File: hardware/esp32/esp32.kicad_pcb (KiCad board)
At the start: 2 copper layers, 22 x 34.2 mm, 15 parts, among them J1 Conn_01x02, J2 Conn_01x02, J3 Conn_01x02, J4 Conn_01x02, J5 Conn_01x02, SW1 RESET, SW2 BOOT, U2 ESP32-S3-MINI-1-N8

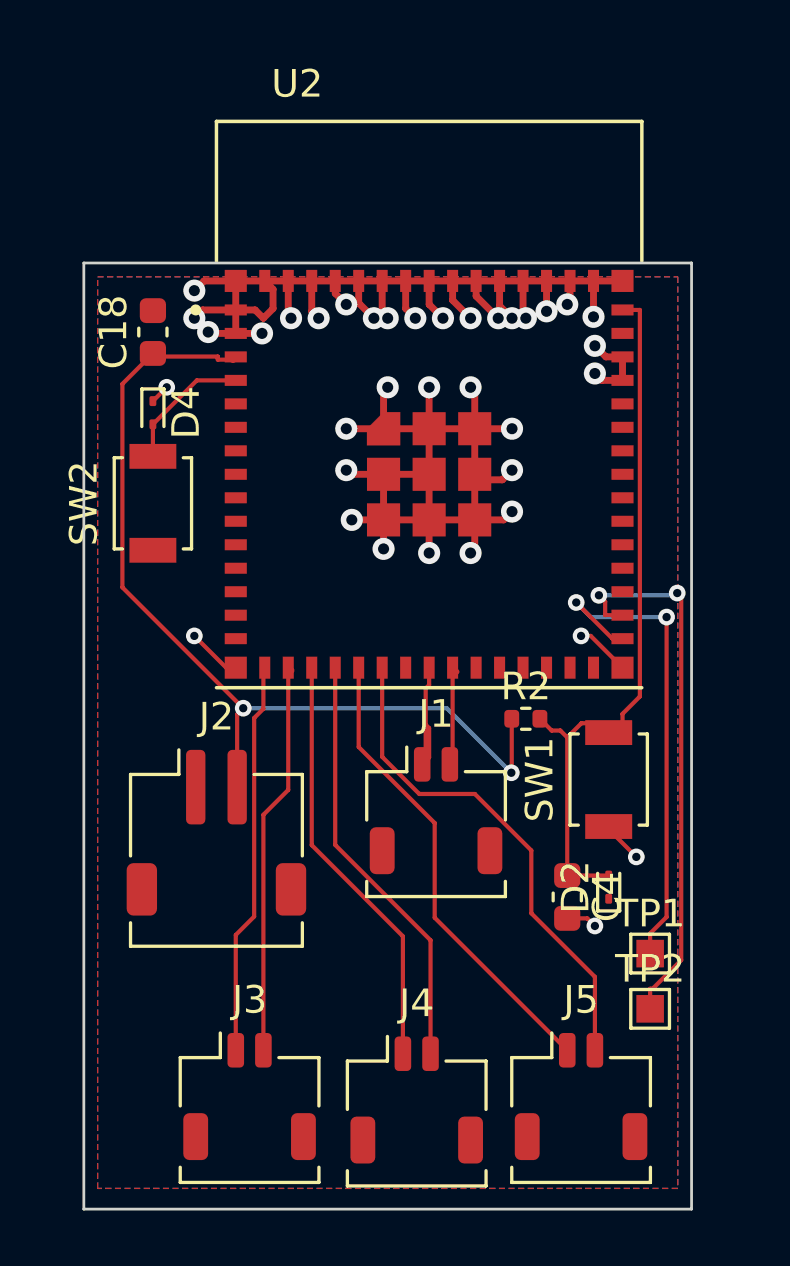
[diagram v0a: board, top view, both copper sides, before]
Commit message: simplify pins and buttons
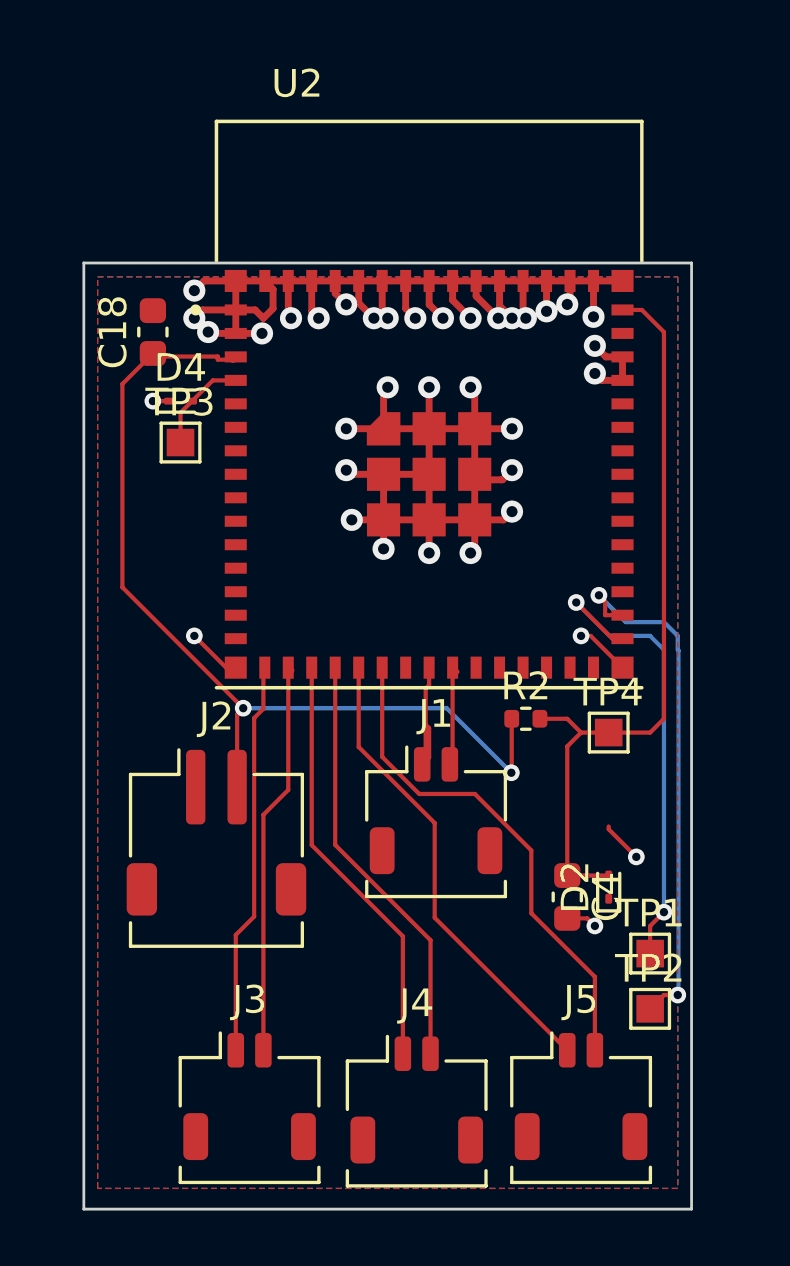
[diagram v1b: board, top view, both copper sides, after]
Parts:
- removed SW1: RESET, Button_Switch_SMD:SW_SPST_B3U-1000P
- removed SW2: BOOT, Button_Switch_SMD:SW_SPST_B3U-1000P
- added TP3: TestPoint, TestPoint:TestPoint_Pad_1.0x1.0mm, F.Cu at (104.0, 39.0)
- added TP4: TestPoint, TestPoint:TestPoint_Pad_1.0x1.0mm, F.Cu at (119.5, 49.5)
- moved D4 1.08 mm to (104.0, 37.5), turned to 0 degrees
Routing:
- net /GPIO0: track 4.82 -> 3.56 mm
- net /ESP32_EN: track 26.6 -> 27.6 mm
- net Net-(U2-IO35): track 18.1 -> 17.3 mm
- net Net-(U2-IO36): track 19.9 -> 19.1 mm

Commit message: esp32 routing
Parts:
- removed J3, J4, J5: Conn_01x02, Connector_JST:JST_SHL_SM02B-SHLS-TF_1x02-1MP_P1.00mm_Horizontal
- removed TP1, TP2: TestPoint, TestPoint:TestPoint_Pad_1.0x1.0mm
- added J6: Conn_01x08, Connector_JST:JST_SHL_SM08B-SHLS-TF_1x08-1MP_P1.00mm_Horizontal, F.Cu at (114.0, 62.7)
- moved C4 2.64 mm to (119.5, 53.3)
- moved D2 2.64 mm to (121.0, 52.9)
- moved R2 2.51 mm to (118.0, 51.0)
- moved TP4 1.58 mm to (121.0, 50.0)
- moved TP3 1.50 mm to (104.0, 40.5)
- moved J1 0.70 mm to (113.5, 51.7)
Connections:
- U2 pad 15: unconnected-(U2-IO11-Pad15) -> Net-(J6-Pin_1)
- U2 pad 22: unconnected-(U2-IO18-Pad22) -> Net-(J6-Pin_8)
- U2 pad 31: Net-(U2-IO35) -> unconnected-(U2-IO35-Pad31)
- U2 pad 32: Net-(U2-IO36) -> unconnected-(U2-IO36-Pad32)
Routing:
- net Net-(J6-Pin_1): track 0.00 -> 28.0 mm, vias 0 -> 2
- net Net-(U2-IO36): track 19.1 -> 0.00 mm, vias 2 -> 0
- net Net-(J6-Pin_8): track 0.00 -> 18.2 mm
- net Net-(U2-IO35): track 17.3 -> 0.00 mm, vias 2 -> 0
- net Net-(J6-Pin_3): track 14.4 -> 18.9 mm, vias 0 -> 2
- net GND: track 86.6 -> 89.7 mm
- net /USB_D-: track 5.02 -> 2.85 mm
- net Net-(J6-Pin_2): track 14.3 -> 16.4 mm
- net Net-(J6-Pin_7): track 18.2 -> 16.4 mm, vias 0 -> 2
- net /ESP32_EN: track 27.6 -> 25.8 mm
- net /GPIO0: track 3.56 -> 5.13 mm
- net Net-(J6-Pin_6): track 17.0 -> 16.0 mm, vias 0 -> 2
- net /USB_D+: track 3.75 -> 3.02 mm
- net +3V3: track 34.1 -> 34.6 mm
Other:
- board size 22 x 34.2 mm -> 21.5 x 34.2 mm

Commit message: esp32
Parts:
- added TP1: TestPoint, MountingHole:MountingHole_2.1mm, F.Cu at (104.5, 62.5)
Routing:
- net Net-(J6-Pin_1): track 28.0 -> 19.3 mm
- net Net-(J6-Pin_3): track 18.9 -> 15.8 mm
- net Net-(J6-Pin_2): track 16.4 -> 15.8 mm
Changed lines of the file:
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@@
 		)
+	)
+	(footprint "MountingHole:MountingHole_2.1mm"
+		(layer "F.Cu")
+		(at 104.5 62.5)
+		(descr "Mounting Hole 2.1mm, no annular, generated by kicad-footprint-generator mountinghole.py")
+		(tags "mountinghole")
+		(property "Reference" "TP1"
+			(at 0 -3.05 0)
+			(layer "F.SilkS")
+			(effects
+				(font
+					(size 1 1)
+					(thickness 0.15)
+				)
+			)
+		)
+		(property "Value" "TestPoint"
+			(at 0 3.05 0)
+			(layer "F.Fab")
+			(effects
+				(font
+					(size 1 1)
+					(thickness 0.15)
+				)
+			)
+		)
+		(property "Datasheet" "~"
+			(at 0 0 0)
+			(layer "F.Fab")
+			(hide yes)
+			(effects
+				(font
+					(size 1.27 1.27)
+					(thickness 0.15)
+				)
+			)
+		)
+		(property "Description" "test point"
+			(at 0 0 0)
+			(layer "F.Fab")
+			(hide yes)
+			(effects
+				(font
+					(size 1.27 1.27)
+					(thickness 0.15)
+				)
+			)
+		)
+		(property ki_fp_filters "Pin* Test*")
+		(sheetname "/")
+		(sheetfile "esp32.kicad_sch")
+		(attr exclude_from_pos_files)
+		(fp_circle
+			(center 0 0)
+			(end 2.1 0)
+			(stroke
+				(width 0.15)
+				(type solid)
+			)
+			(fill no)
+			(layer "Cmts.User")
+		)
+		(fp_circle
+			(center 0 0)
+			(end 2.35 0)
+			(stroke
+				(width 0.05)
+				(type solid)
+			)
+			(fill no)
+			(layer "F.CrtYd")
+		)
+		(fp_text user "${REFERENCE}"
+			(at 0 0 0)
+			(layer "F.Fab")
+			(effects
+				(font
+					(size 1 1)
+					(thickness 0.15)
+				)
+			)
+		)
+		(pad "" np_thru_hole circle
+			(at 0 0)
+			(size 2.1 2.1)
+			(drill 2.1)
+			(layers "*.Cu" "*.Mask")
+		)
+		(embedded_fonts no)
 	)
 	(footprint "Capacitor_SMD:C_0603_1608Metric"
@@
 	)
 	(segment
-		(start 109.4586 65.2609)
-		(end 108.6816 65.2609)
-		(width 0.1524)
-		(layer "F.Cu")
-		(net 33)
-	)
-	(segment
-		(start 110.5 64.2195)
-		(end 109.4586 65.2609)
-		(width 0.1524)
-		(layer "F.Cu")
-		(net 33)
-	)
-	(segment
 		(start 105.1348 45.5244)
 		(end 105.3721 45.7617)
@@
 	)
 	(segment
-		(start 108.6816 65.2609)
-		(end 105.3304 61.9097)
-		(width 0.1524)
-		(layer "F.Cu")
-		(net 33)
-	)
-	(segment
 		(start 105.3721 45.7617)
 		(end 105.3721 46.1)
@@
 	)
 	(segment
-		(start 110.5 61)
-		(end 110.5 64.2195)
+		(start 109.5 60)
+		(end 110.5 61)
 		(width 0.1524)
 		(layer "F.Cu")
@@
 	)
 	(segment
-		(start 105.3304 61.9097)
-		(end 105.3304 49.1591)
+		(start 109 60)
+		(end 109.5 60)
 		(width 0.1524)
 		(layer "F.Cu")
@@
 	)
 	(via
-		(at 105.3304 49.1591)
-		(size 0.6048)
+		(at 109 60)
+		(size 0.604799)
 		(drill 0.299999)
 		(layers "F.Cu" "B.Cu")
@@
 	)
 	(segment
-		(start 105.1348 48.9635)
-		(end 105.1348 45.5244)
+		(start 105.1348 45.5244)
+		(end 105.1348 56.1348)
 		(width 0.1524)
 		(layer "B.Cu")
@@
 	)
 	(segment
-		(start 105.3304 49.1591)
-		(end 105.1348 48.9635)
+		(start 105.1348 56.1348)
+		(end 107 58)
 		(width 0.1524)
 		(layer "B.Cu")
@@
 	)
 	(segment
-		(start 110.9374 59.3774)
-		(end 111.5 59.3774)
+		(start 107 58)
+		(end 109 60)
+		(width 0.1524)
+		(layer "B.Cu")
+		(net 33)
+	)
+	(segment
+		(start 107.05 55.9304)
+		(end 111.5 60.3804)
 		(width 0.1524)
 		(layer "F.Cu")
@@
 	)
 	(segment
-		(start 111.5 59.3774)
+		(start 111.5 60.3804)
 		(end 111.5 61)
-		(width 0.1524)
-		(layer "F.Cu")
-		(net 34)
-	)
-	(segment
-		(start 110.56 59)
-		(end 110.9374 59.3774)
-		(width 0.1524)
-		(layer "F.Cu")
-		(net 34)
-	)
-	(segment
-		(start 107.05 55.9304)
-		(end 110.12 59)
 		(width 0.1524)
 		(layer "F.Cu")
@@
 	)
 	(segment
-		(start 110.12 59)
-		(end 110.56 59)
-		(width 0.1524)
-		(layer "F.Cu")
-		(net 34)
-	)
-	(segment
 		(start 108 50.3314)
 		(end 108 47.25)
@@
 	)
 	(segment
-		(start 108 53.3759)
-		(end 108 53.294)
-		(width 0.1524)
-		(layer "F.Cu")
-		(net 35)
-	)
-	(segment
 		(start 112.5 59.2816)
 		(end 112.5 61)
@@
 	)
 	(segment
-		(start 108 53.2913)
-		(end 108 53.2068)
-		(width 0.1524)
-		(layer "F.Cu")
-		(net 35)
-	)
-	(segment
-		(start 108 53.2068)
-		(end 108 50.3314)
-		(width 0.1524)
-		(layer "F.Cu")
-		(net 35)
-	)
-	(segment
 		(start 107.9 50.4314)
 		(end 107.9 51.06)
 		(width 0.1524)
 		(layer "F.Cu")
-		(net 35)
-	)
-	(segment
-		(start 108 53.294)
-		(end 108 53.2913)
-		(width 0.1524)
-		(layer "F.Cu")

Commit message: esp32 rebuild connectors
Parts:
- removed J1: Conn_01x02, Connector_JST:JST_SHL_SM02B-SHLS-TF_1x02-1MP_P1.00mm_Horizontal
- removed J6: Conn_01x08, Connector_JST:JST_SHL_SM08B-SHLS-TF_1x08-1MP_P1.00mm_Horizontal
- removed TP1: TestPoint, MountingHole:MountingHole_2.1mm
- added J3: Conn_01x10, Connector_JST:JST_SHL_SM10B-SHLS-TF_1x10-1MP_P1.00mm_Horizontal, F.Cu at (115.5, 57.5)
- moved J2 3.37 mm to (104.8, 56.5)
- moved C4 3.04 mm to (119.0, 50.3)
- moved D2 0.92 mm to (120.9, 52.0), turned to 0 degrees
- moved R2 0.51 mm to (117.5, 51.0), turned to 90 degrees
- moved TP4 0.50 mm to (121.0, 50.5)
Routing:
- net /USB_D+: track 3.02 -> 11.4 mm
- net /USB_D-: track 2.85 -> 11.1 mm
- net Net-(J3-Pin_8): track 18.2 -> 11.1 mm
- net +3V3: track 34.6 -> 40.5 mm
- net Net-(J3-Pin_7): track 16.4 -> 11.0 mm, vias 2 -> 0
- net Net-(J3-Pin_1): track 19.3 -> 14.2 mm, vias 2 -> 0
- net Net-(J3-Pin_6): track 16.0 -> 10.9 mm, vias 2 -> 0
- net Net-(J3-Pin_2): track 15.8 -> 10.7 mm
- net Net-(J3-Pin_4): track 15.8 -> 10.8 mm
- net Net-(J3-Pin_5): track 15.9 -> 10.9 mm
- net Net-(J3-Pin_3): track 15.8 -> 10.9 mm, vias 2 -> 0
- net /ESP32_EN: track 25.8 -> 23.8 mm
- net GND: track 89.7 -> 91.3 mm
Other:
- board size 21.5 x 34.2 mm -> 22.5 x 29.8 mm

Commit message: some fixes
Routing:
- net GND: track 91.3 -> 93.1 mm
- net +3V3: track 40.5 -> 41.4 mm
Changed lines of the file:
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@@
 		(start 120.5 53)
 		(end 121 53.5)
-		(width 0.1524)
+		(width 0.3)
 		(layer "F.Cu")
 		(net 1)
@@
 		(start 119.95 52)
 		(end 119 51.05)
-		(width 0.1524)
+		(width 0.3)
 		(layer "F.Cu")
 		(net 1)
@@
 	)
 	(segment
+		(start 103.775 34.225)
+		(end 104.5 33.5)
+		(width 0.1524)
+		(layer "F.Cu")
+		(net 1)
+	)
+	(segment
 		(start 104.8 34.2)
 		(end 104.5 34.5)
@@
 	)
 	(segment
+		(start 103 34.225)
+		(end 103.775 34.225)
+		(width 0.1524)
+		(layer "F.Cu")
+		(net 1)
+	)
+	(segment
 		(start 118.1 33.15)
 		(end 118.95 33.15)
@@
 		(start 120.5 52)
 		(end 119.95 52)
-		(width 0.1524)
+		(width 0.3)
 		(layer "F.Cu")
 		(net 1)
@@
 		(start 102.5 53.3)
 		(end 102.5 52.5)
-		(width 0.1524)
+		(width 0.5)
 		(layer "F.Cu")
 		(net 1)
@@
 		(start 120.5 52)
 		(end 120.5 53)
-		(width 0.1524)
+		(width 0.3)
 		(layer "F.Cu")
 		(net 1)
@@
 		(start 104 54.8)
 		(end 102.5 53.3)
-		(width 0.1524)
+		(width 0.5)
 		(layer "F.Cu")
 		(net 1)
@@
 	)
 	(segment
-		(start 105.2129 52.9724)
+		(start 102 50)
+		(end 104.9724 52.9724)
+		(width 0.4)
+		(layer "F.Cu")
+		(net 32)
+	)
+	(segment
+		(start 105.5 54.8)
 		(end 105.5 53.2595)
-		(width 0.1524)
-		(layer "F.Cu")
-		(net 32)
-	)
-	(segment
-		(start 105.95 35.95)
-		(end 106 35.9)
-		(width 0.25)
-		(layer "F.Cu")
-		(net 32)
-	)
-	(segment
-		(start 103.275 35.95)
-		(end 103.225 36)
-		(width 0.1524)
-		(layer "F.Cu")
-		(net 32)
-	)
-	(segment
-		(start 105.5 53.2595)
-		(end 105.5 53.5257)
-		(width 0.1524)
-		(layer "F.Cu")
-		(net 32)
-	)
-	(segment
-		(start 103.225 36)
-		(end 103.112 35.8877)
-		(width 0.1524)
-		(layer "F.Cu")
-		(net 32)
-	)
-	(segment
-		(start 103.112 35.8875)
-		(end 103 35.775)
-		(width 0.1524)
-		(layer "F.Cu")
-		(net 32)
-	)
-	(segment
-		(start 117.5 51.6667)
-		(end 119.223 53.3897)
-		(width 0.1524)
-		(layer "F.Cu")
-		(net 32)
-	)
-	(segment
-		(start 105.5 53.5257)
-		(end 105.5 54.8)
-		(width 0.1524)
-		(layer "F.Cu")
-		(net 32)
-	)
-	(segment
-		(start 103.112 35.8877)
-		(end 103.112 35.8875)
-		(width 0.1524)
+		(width 0.5)
+		(layer "F.Cu")
+		(net 32)
+	)
+	(segment
+		(start 106 35.9)
+		(end 103.125 35.9)
+		(width 0.4)
+		(layer "F.Cu")
+		(net 32)
+	)
+	(segment
+		(start 102 36.775)
+		(end 102 50)
+		(width 0.4)
 		(layer "F.Cu")
 		(net 32)
@@
 	(segment
 		(start 103 35.775)
-		(end 103 35.7755)
-		(width 0.1524)
-		(layer "F.Cu")
-		(net 32)
-	)
-	(segment
-		(start 103 50.7595)
-		(end 103 35.7755)
-		(width 0.1524)
-		(layer "F.Cu")
-		(net 32)
-	)
-	(segment
-		(start 105.2129 52.9724)
-		(end 103 50.7595)
-		(width 0.1524)
-		(layer "F.Cu")
-		(net 32)
-	)
-	(segment
-		(start 105.9 36)
-		(end 105.95 35.95)
-		(width 0.25)
+		(end 102 36.775)
+		(width 0.4)
+		(layer "F.Cu")
+		(net 32)
+	)
+	(segment
+		(start 117.5191 51.52)
+		(end 119.3888 53.3897)
+		(width 0.4)
+		(layer "F.Cu")
+		(net 32)
+	)
+	(segment
+		(start 117.5 51.52)
+		(end 117.5191 51.52)
+		(width 0.1524)
 		(layer "F.Cu")
 		(net 32)
@@
 	)
 	(segment
-		(start 103 35.7755)
-		(end 103.112 35.8877)
-		(width 0.1524)
+		(start 104.9724 52.9724)
+		(end 105.2129 52.9724)
+		(width 0.4)
+		(layer "F.Cu")
+		(net 32)
+	)
+	(segment
+		(start 103.125 35.9)
+		(end 103 35.775)
+		(width 0.4)
+		(layer "F.Cu")
+		(net 32)
+	)
+	(segment
+		(start 105.5 53.2595)
+		(end 105.2129 52.9724)
+		(width 0.5)
 		(layer "F.Cu")
 		(net 32)
@@
 		(start 119.223 53.3897)
 		(end 119.3888 53.3897)
-		(width 0.1524)
-		(layer "F.Cu")
-		(net 32)
-	)
-	(segment
-		(start 105.95 35.95)
-		(end 103.275 35.95)
 		(width 0.1524)
 		(layer "F.Cu")
@@
 	)
 	(segment
-		(start 105.6302 53.3897)
-		(end 105.2129 52.9724)
-		(width 0.1524)
+		(start 105.2129 52.9724)
+		(end 118.9715 52.9724)
+		(width 0.4)
 		(layer "B.Cu")
 		(net 32)
 	)
 	(segment
-		(start 119.3888 53.3897)
-		(end 105.6302 53.3897)
-		(width 0.1524)
+		(start 118.9715 52.9724)
+		(end 119.3888 53.3897)
+		(width 0.4)
 		(layer "B.Cu")
 		(net 32)

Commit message: wip
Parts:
- removed TP3, TP4: TestPoint, TestPoint:TestPoint_Pad_1.0x1.0mm
- added J1: Conn_01x01, Connector_PinHeader_1.00mm:PinHeader_1x01_P1.00mm_Vertical, F.Cu at (121.0, 50.5)
- added J6: Conn_01x01, Connector_PinHeader_1.00mm:PinHeader_1x01_P1.00mm_Vertical, F.Cu at (103.5, 40.5)
- D2, D4: footprint Diode_SMD:D_SOD-923 -> Package_TO_SOT_SMD:SOT-723
- moved D2 1.65 mm to (121.4, 53.6), turned to -90 degrees
- moved D4 0.50 mm to (103.5, 37.5), turned to 90 degrees
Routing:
- net GND: track 93.1 -> 91.4 mm, vias 37 -> 38
- net /ESP32_EN: track 23.8 -> 24.7 mm

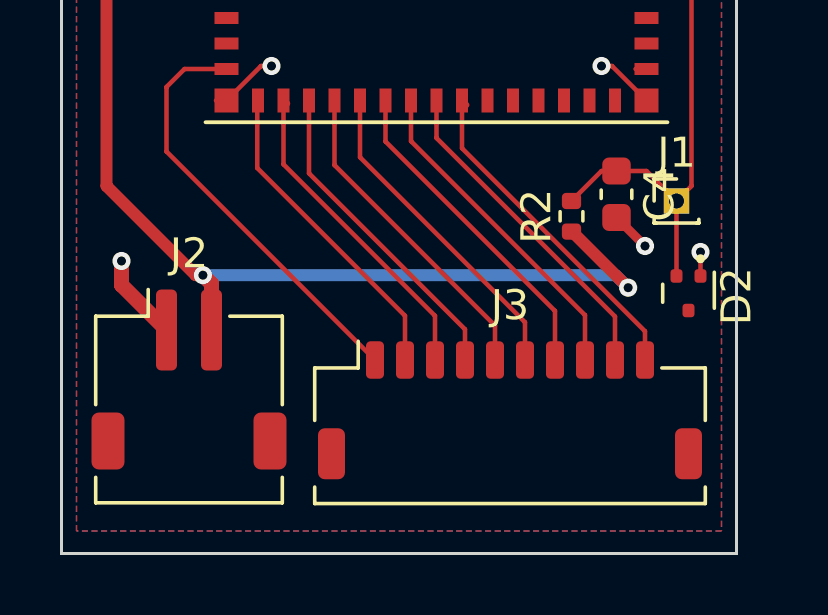
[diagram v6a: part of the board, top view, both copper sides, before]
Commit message: replace connectors
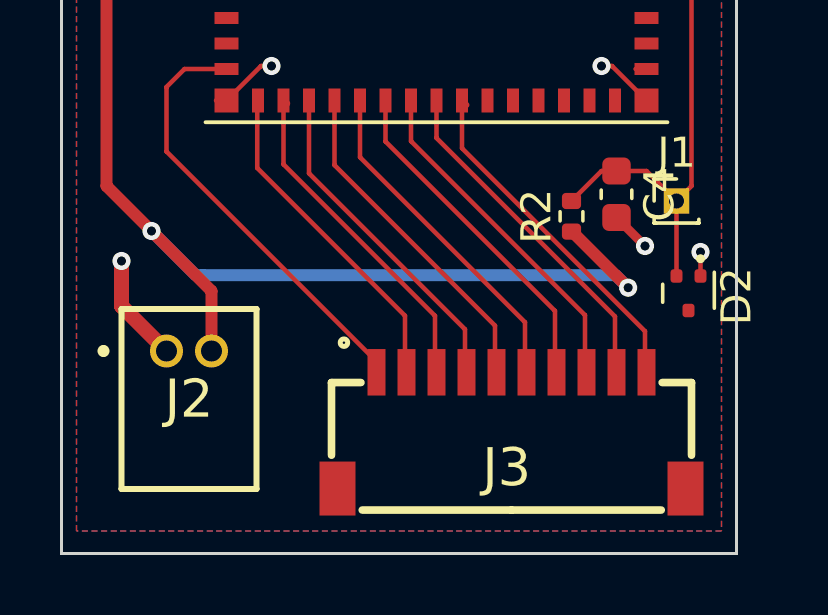
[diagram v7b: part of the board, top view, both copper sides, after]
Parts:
- J2: footprint Connector_JST:JST_ZH_S2B-ZR-SM4A-TF_1x02-1MP_P1.50mm_Horizontal -> LIB_S2B-ZR_LF__SN_:S2BZRLFSN
- J3: footprint Connector_JST:JST_SHL_SM10B-SHLS-TF_1x10-1MP_P1.00mm_Horizontal -> LIB_SM10B-SRSS-TB_LF__SN_:SM10B-SRSS-TB
- moved J3 6.02 mm to (109.5, 56.6)
- moved J2 1.21 mm to (104.0, 55.5)
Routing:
- net +3V3: track 41.4 -> 44.3 mm
- net GND: track 91.4 -> 92.1 mm
